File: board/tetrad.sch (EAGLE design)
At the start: 128 parts, among them Q1 FET-PCH-TO252, Q10 FET-NCH-SOT23, Q11 FET-NCH-SOT23, Q12 FET-NCH-SOT23, Q2 FET-NCH-SOT23, Q3 FET-NCH-SOT23, Q4 FET-NCH-SOT23, Q5 FET-NCH-SOT23, Q6 FET-NCH-SOT23, Q7 FET-NCH-SOT23, Q8 FET-NCH-SOT23, Q9 FET-NCH-SOT23, U1 IO-MCP23017ML, U2 RADIO-ESP32_DEVKIT, U3 R-78E5.0-1.0

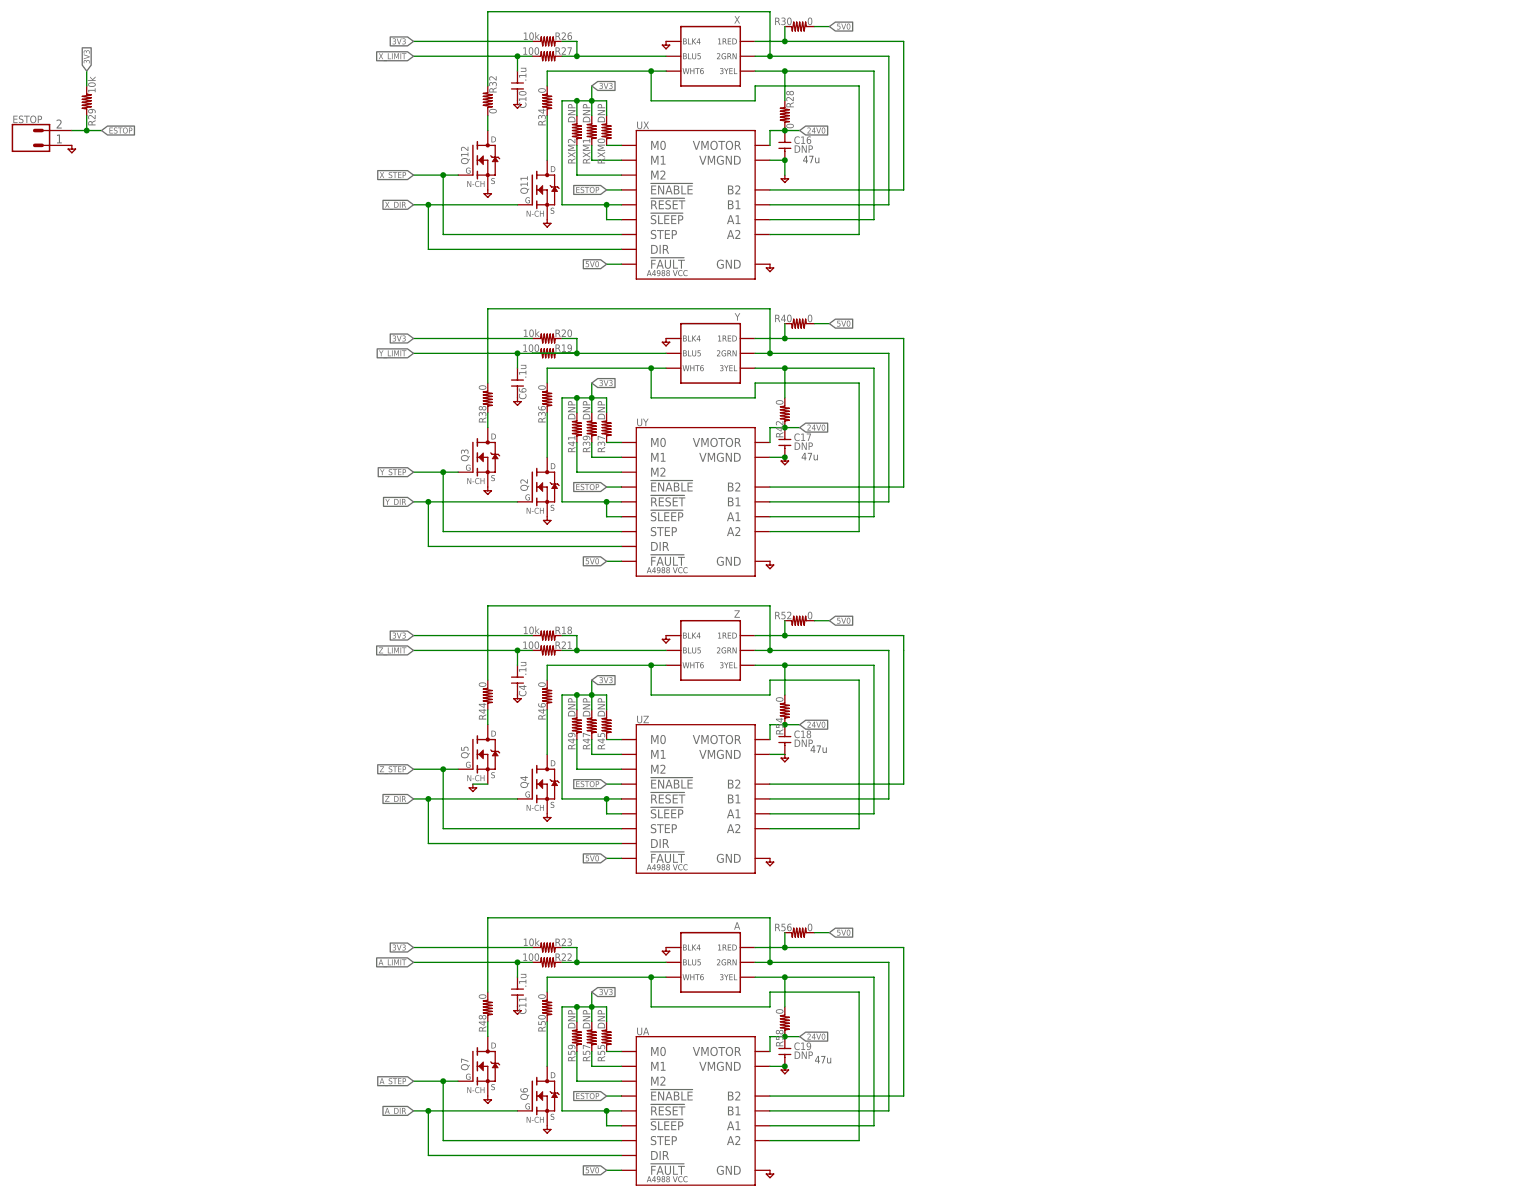
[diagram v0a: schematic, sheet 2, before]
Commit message: checked out the spindle hardware started to simplify the motor part of schematic
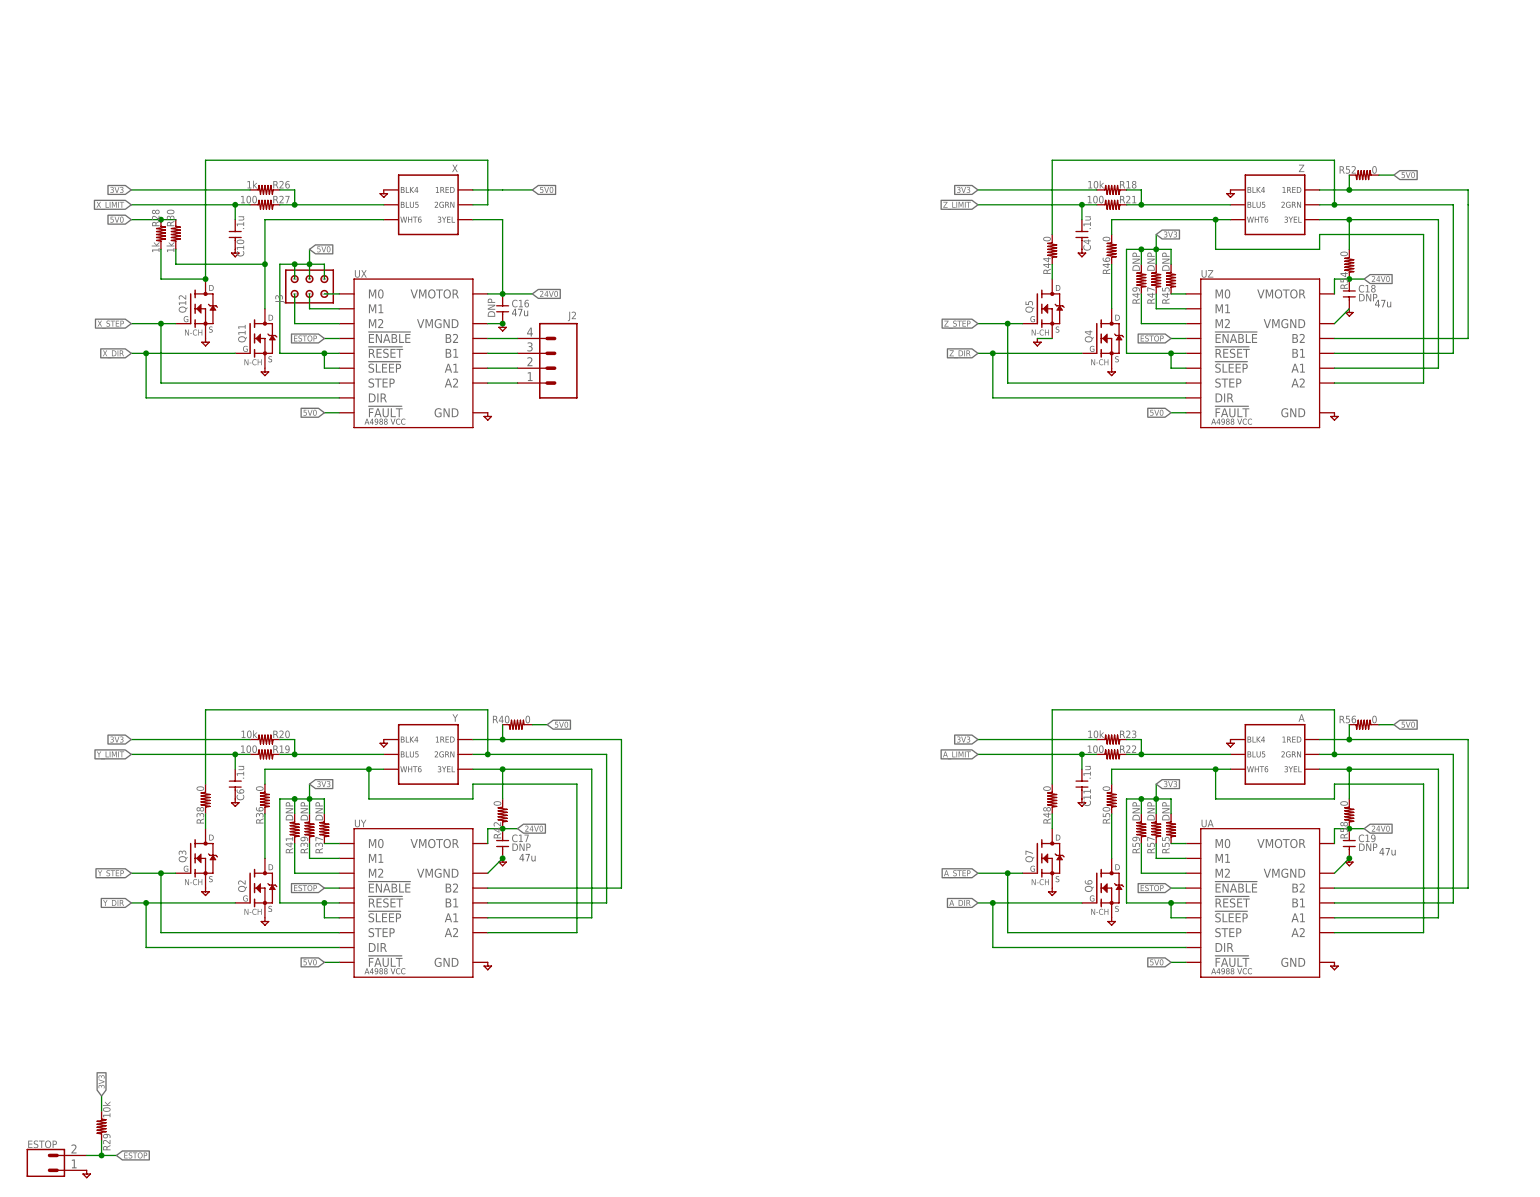
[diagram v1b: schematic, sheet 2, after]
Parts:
- removed R32, R34: 0, holla:R-0603
- removed RXM0, RXM1, RXM2: DNP, holla:R-0603
- added F1: 10A, holla:FUSE-HOLDER-3557-2
- added J2: (no value), holla:CONN-04-.100-VERT-HEADER
- added J3: (no value), holla:CONN-03X2-RH
- R26: value 10k -> 1k
- R28, R30: value 0 -> 1k
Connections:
- removed net N$30: R28.1, UX.A1, X.3
- removed net N$32: R30.1, UX.B2, X.1
- removed net N$44: Q12.D, R32.2
- new net N$57: F1.P$2, Q1.D
- new net N$62: J2.2, UX.A1
- new net N$63: J2.3, UX.B1
- new net N$64: J2.4, UX.B2
- net 24V0: now also X.3; no longer R28.2
- net 3V3: no longer RXM0.2, RXM1.2, RXM2.2, UX.!RESET, UX.!SLEEP
- net 5V0: now also J3.2, J3.4, J3.6, R28.1, R30.1, UX.!RESET, UX.!SLEEP, X.1; no longer R30.2
- net N$1: now also F1.P$1; no longer Q1.D
- net N$25: now also J2.1; no longer R34.2, X.6
- net N$31: now also Q12.D, R28.2; no longer R32.1, UX.B1
- net N$33: now also J3.5; no longer RXM0.1
- net N$34: now also J3.3; no longer RXM1.1
- net N$35: now also J3.1; no longer RXM2.1
- net N$5: now also R30.2, X.6; no longer R34.1
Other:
- note added: "todo add EVE2 display connector CS_SD is on an input only pin, fix this replace esp32 with new lib part, reroute check audio pin on FFC connector https://randomnerdtutorials.com/esp32-pinout-reference-gpios/ check if D14 and D15 PWM out on startup add 0430450612 headers add drv8825 board headers switch 23017 to qfn add strong pull ups to steps and dir add high current N-CH to extra 23107 outputs 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"
- note removed: "todo add EVE2 display connector CS_SD is on an input only pin, fix this replace esp32 with new lib part, reroute check audio pin on FFC connector https://randomnerdtutorials.com/esp32-pinout-reference-gpios/ check if D14 and D15 PWM out on startup add 0430450612 headers add drv8825 board headers switch 23017 to qfn add strong pull ups to steps and dir add high current N-CH to extra 23107 outputs"
- moved on the sheet: A, C10, C11, C14, C15, C16, C17, C18, C19, C4, C6, D1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

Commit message: schematic   updated alot   moving to bud PN-1325-DGMB enclosure initial add for others
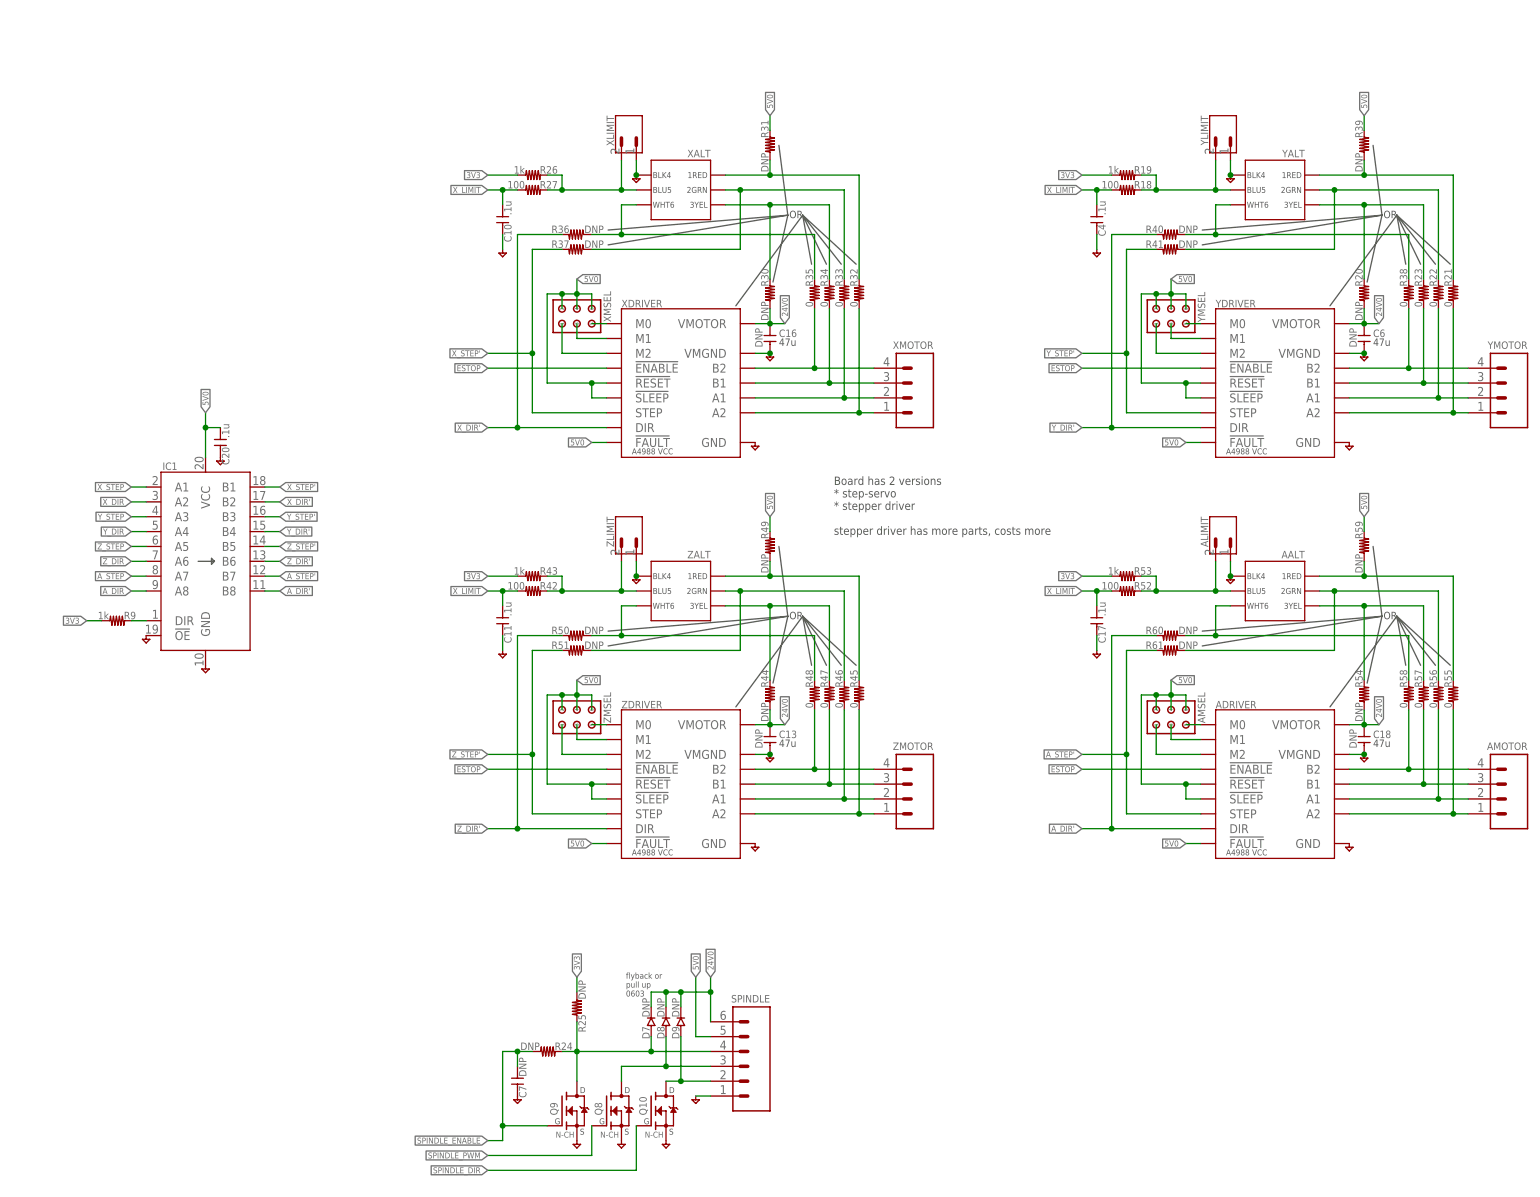
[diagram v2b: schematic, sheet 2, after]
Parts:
- removed 3V3: (no value), holla:TESTPOINTTHRU
- removed A, X, Y, Z: (no value), holla:CONN-03X2-MICROFIT-TH-SMD
- removed C19: DNP, holla:C-1206
- removed DISPLAY: (no value), holla:DISP-SPI-TFT-128X160-ST7735
- removed J3: (no value), holla:CONN-03X2-RH
- removed Q11, Q12, Q6, Q7: FET-NCH-SOT23, holla:FET-NCH-SOT23
- removed UA, UX, UY, UZ: (no value), holla:BOARD-DRV8825-CARRIER-TH-SMD
- added AALT, XALT, YALT, ZALT: (no value), holla:CONN-03X2-MICROFIT-TH-SMD
- added ADRIVER, XDRIVER, YDRIVER, ZDRIVER: (no value), holla:BOARD-DRV8825-CARRIER-TH-SMD
- added ALIMIT, XLIMIT, YLIMIT, ZLIMIT: (no value), holla:CONN-02-.100-VERT-HEADER
- added AMOTOR, XMOTOR, YMOTOR, ZMOTOR: (no value), holla:CONN-04-.100-VERT-HEADER
- added AMSEL, XMSEL, YMSEL, ZMSEL: (no value), holla:CONN-03X2-RH
- added AUDIO: (no value), holla:TESTPOINTTHRU
- added C20: .1u, holla:C-0603
- added D3, D4, D5, D6: (no value), holla:DIODE-0603-SOD523
- added D7, D8, D9: DNP, holla:DIODE-0603-SOD523
- added IC1: (no value), holla:74LS245DW
- added J16: (no value), holla:CONN-05X2-SHD
- added R31, R51, R60, R61: DNP, holla:R-0603
- added R32, R33, R34, R35: 0, holla:R-0603
- added R43, R53: 1k, holla:R-0603
- added U13: (no value), holla:CONN-20-FPC-0.50MM-10051922-2010ELF
- C1, C9: value 1u -> .1u
- C13: value 1u -> DNP; device holla:C-0603 -> holla:C-1206
- C17: value DNP -> .1u; device holla:C-1206 -> holla:C-0603
- C6: value .1u -> DNP; device holla:C-0603 -> holla:C-1206
- J2: device holla:CONN-04-.100-VERT-HEADER -> holla:CONN-06-3.81MM-PLUGIN-SCREW
- Q2, Q3, Q4, Q5: value FET-NCH-SOT23 -> FET-NCH-TO252; device holla:FET-NCH-SOT23 -> holla:FET-NCH-TO252
- R18: value 10k -> 100
- R19, R9: value 100 -> 1k
- R20: value 10k -> DNP
- R21, R22, R8: value 100 -> 0
- R23: value 10k -> 0
- R28: value 1k -> 100
- R30: value 1k -> DNP
- R36, R40, R44, R50, R54: value 0 -> DNP
- R42, R52: value 0 -> 100
- R45, R47, R55, R57: value DNP -> 0
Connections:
- new net A_DIR': ADRIVER.DIR, IC1.B8, R60.1
- new net A_STEP': ADRIVER.STEP, IC1.B7, R61.1
- new net N$108: R8.2, U13.3, U13.4
- new net N$30: D5.A, J2.3, Q4.D
- new net N$32: D4.A, J2.4, Q3.D
- new net N$44: D3.A, J2.5, Q2.D
- new net N$61: ADRIVER.M1, AMSEL.3
- new net N$65: ADRIVER.A1, AMOTOR.2, R56.2
- new net N$66: ADRIVER.B1, AMOTOR.3, R57.2
- new net N$67: ADRIVER.B2, AMOTOR.4, R58.2
- new net N$68: AALT.5, ALIMIT.2, R52.1, R53.1
- new net N$69: AALT.6, R58.1, R60.2
- new net N$70: AALT.1, R55.1, R59.2
- new net N$71: AALT.3, R54.1, R57.1
- new net X_DIR': IC1.B2, R36.1, XDRIVER.DIR
- new net X_STEP': IC1.B1, R22.1, R33.1, R37.1, R37.2, R41.2, R46.1, R51.2, XALT.2, XDRIVER.STEP, YALT.2, ZALT.2
- new net X_STEP'1: AALT.2, R56.1, R61.2
- new net Y_DIR': IC1.B4, R40.1, YDRIVER.DIR
- new net Y_STEP': IC1.B3, R41.1, YDRIVER.STEP
- new net Z_DIR': IC1.B6, R50.1, ZDRIVER.DIR
- new net Z_STEP': IC1.B5, R51.1, ZDRIVER.STEP
- net 24V0: now also ADRIVER.VMOTOR, C13.1, C6.1, D3.C, D4.C, D5.C, D6.C, D7.C, D8.C, D9.C, J2.6, R20.2, R30.2, R44.2, R54.2, XDRIVER.VMOTOR, YDRIVER.VMOTOR, ZDRIVER.VMOTOR; no longer C17.1, C19.1, R42.1, R54.1, R58.1, UA.VMOTOR, UX.VMOTOR, UY.VMOTOR, UZ.VMOTOR, X.3
- net 3V3: now also C1.1, C9.1, J16.1, R19.2, R43.2, R53.2, R8.1, R9.2, U13.20, U13.5; no longer 3V3.P$1, C1.2, C13.2, C9.2, R18.2, R20.2, R23.2, R37.2, R39.2, R41.2, R45.2, R47.2, R49.2, R55.2, R57.2, R59.2, UA.!RESET, UA.!SLEEP, UY.!RESET, UY.!SLEEP, UZ.!RESET, UZ.!SLEEP
- net 5V0: now also ADRIVER.!FAULT, ADRIVER.!RESET, ADRIVER.!SLEEP, AMSEL.2, AMSEL.4, AMSEL.6, C20.1, IC1.VCC, R31.1, R39.1, R49.1, R59.1, XDRIVER.!FAULT, XDRIVER.!RESET, XDRIVER.!SLEEP, XMSEL.2, XMSEL.4, XMSEL.6, YDRIVER.!FAULT, YDRIVER.!RESET, YDRIVER.!SLEEP, YMSEL.2, YMSEL.4, YMSEL.6, ZDRIVER.!FAULT, ZDRIVER.!RESET, ZDRIVER.!SLEEP, ZMSEL.2, ZMSEL.4, ZMSEL.6; no longer DISPLAY.VCC, J3.2, J3.4, J3.6, R28.1, R30.1, R40.2, R52.2, R56.2, UA.!FAULT, UX.!FAULT, UX.!RESET, UX.!SLEEP, UY.!FAULT, UZ.!FAULT, X.1
- net AUDIO: now also AUDIO.P$1, J16.9, U13.11
- net A_DIR: now also IC1.A8; no longer Q6.G, UA.DIR
- net A_LIMIT: no longer C11.1, R22.2
- net A_STEP: now also IC1.A7; no longer Q7.G, UA.STEP
- net CS_DISPLAY: now also J16.6, U13.15
- net CYCLE_START: now also U2.D39_IN_ONLY/VN; no longer U2.D39/VN
- net DISPLAY_CS: no longer DISPLAY.CS
- net DISPLAY_DC: no longer DISPLAY.DC
- net ESTOP: now also ADRIVER.!ENABLE, R28.1, XDRIVER.!ENABLE, YDRIVER.!ENABLE, ZDRIVER.!ENABLE; no longer UA.!ENABLE, UX.!ENABLE, UY.!ENABLE, UZ.!ENABLE
- net FEED_HOLD: now also U2.D36_IN_ONLY/VP; no longer U2.D36/VP
- net GND: now also AALT.4, ADRIVER.GND, ADRIVER.VMGND, ALIMIT.1, C1.2, C13.2, C20.2, C9.2, IC1.!OE, IC1.GND, J16.10, J16.2, J2.1, U13.1, U13.19, U13.2, U13.6, U13.G, XALT.4, XDRIVER.GND, XDRIVER.VMGND, XLIMIT.1, YALT.4, YDRIVER.GND, YDRIVER.VMGND, YLIMIT.1, ZALT.4, ZDRIVER.GND, ZDRIVER.VMGND, ZLIMIT.1; no longer A.4, C1.1, C13.1, C19.2, C9.1, DISPLAY.GND, Q11.S, Q12.S, Q6.S, Q7.S, UA.GND, UA.VMGND, UX.GND, UX.VMGND, UY.GND, UY.VMGND, UZ.GND, UZ.VMGND, X.4, Y.4, Z.4
- net INT_DISPLAY: now also J16.7, U13.14
- net MISO: now also J16.4, U13.17
- net MOSI: now also J16.5, U13.16; no longer R8.2
- net N$10: now also R22.2, YDRIVER.A1, YMOTOR.2; no longer A.5, R22.1, R23.1
- net N$11: now also R23.2, YDRIVER.B1, YMOTOR.3; no longer Q7.D, R48.1
- net N$13: now also D7.A
- net N$14: now also D9.A
- net N$18: now also R1.1
- net N$19: now also R7.1
- net N$2: now also R30.1, R34.1, XALT.3; no longer R26.1, R27.1, X.5
- net N$20: now also D6.A, J2.2, Q5.D; no longer DISPLAY.BL
- net N$21: now also R38.2, YDRIVER.B2, YMOTOR.4; no longer Q3.D, R38.1
- net N$25: now also R32.2, XDRIVER.A2, XMOTOR.1; no longer J2.1, UX.A2
- net N$3: now also IC1.DIR; no longer DISPLAY.SCLK
- net N$31: now also R18.1, R19.1, YALT.5, YLIMIT.2; no longer Q12.D, R28.2, X.2
- net N$33: now also XDRIVER.M0, XMSEL.5; no longer J3.5, UX.M0
- net N$34: now also XDRIVER.M1, XMSEL.3; no longer J3.3, UX.M1
- net N$35: now also XDRIVER.M2, XMSEL.1; no longer J3.1, UX.M2
- net N$36: now also R38.1, R40.2, YALT.6; no longer Q6.D, R50.1
- net N$37: now also R21.1, R39.2, YALT.1; no longer R37.1, UY.M0
- net N$38: now also R20.1, R23.1, YALT.3; no longer R39.1, UY.M1
- net N$39: now also R45.2, ZDRIVER.A2, ZMOTOR.1; no longer R41.1, UY.M2
- net N$4: now also R28.2; no longer DISPLAY.MOSI, R8.1
- net N$40: now also ZDRIVER.M0, ZMSEL.5; no longer R36.2, UY.A2, Y.6
- net N$41: now also ZDRIVER.M1, ZMSEL.3; no longer R42.2, UY.A1, Y.3
- net N$42: now also ZDRIVER.M2, ZMSEL.1; no longer R38.2, UY.B1, Y.2
- net N$43: now also R46.2, ZDRIVER.A1, ZMOTOR.2; no longer R40.1, UY.B2, Y.1
- net N$45: now also R47.2, ZDRIVER.B1, ZMOTOR.3; no longer R55.1, UA.M0
- net N$46: now also R48.2, ZDRIVER.B2, ZMOTOR.4; no longer R45.1, UZ.M0
- net N$47: now also R42.1, R43.1, ZALT.5, ZLIMIT.2; no longer R47.1, UZ.M1
- net N$48: now also R48.1, R50.2, ZALT.6; no longer R49.1, UZ.M2
- net N$49: now also R45.1, R49.2, ZALT.1; no longer R57.1, UA.M1
- net N$5: now also R31.2, R32.1, XALT.1; no longer Q11.D, R30.2, X.6
- net N$50: now also R47.1, ZALT.3; no longer Q5.D
- net N$51: now also ADRIVER.A2, AMOTOR.1, R55.2; no longer R46.2, UZ.A2, Z.6
- net N$52: now also Q2.G, U1.GPB4; no longer Q4.D, R46.1
- net N$53: now also Q3.G, U1.GPB5; no longer R44.2, UZ.B1, Z.2
- net N$54: now also Q4.G, U1.GPB6; no longer R54.2, UZ.A1, Z.3
- net N$55: now also Q5.G, U1.GPB7; no longer R59.1, UA.M2
- net N$56: now also R35.2, XDRIVER.B2, XMOTOR.4; no longer R52.1, UZ.B2, Z.1
- net N$58: now also R26.1, R27.1, XALT.5, XLIMIT.2; no longer A.6, R50.2, UA.A2
- net N$59: now also ADRIVER.M0, AMSEL.5; no longer A.3, R58.2, UA.A1
- net N$6: now also R21.2, YDRIVER.A2, YMOTOR.1; no longer R19.1, R20.1, Y.5
- net N$60: now also R35.1, R36.2, XALT.6; no longer A.2, R48.2, UA.B1
- net N$62: now also R33.2, XDRIVER.A1, XMOTOR.2; no longer J2.2, UX.A1
- net N$63: now also R34.2, XDRIVER.B1, XMOTOR.3; no longer J2.3, UX.B1
- net N$64: now also ADRIVER.M2, AMSEL.1; no longer J2.4, UX.B2
- net N$7: now also YDRIVER.M0, YMSEL.5; no longer Q2.D, R36.1
- net N$8: now also YDRIVER.M1, YMSEL.3; no longer R18.1, R21.1, Z.5
- net N$9: now also YDRIVER.M2, YMSEL.1; no longer A.1, R56.1, UA.B2
- net PD_DISPLAY: now also J16.8, U13.13
- net RESET: no longer DISPLAY.RESET
- net SCK: now also J16.3, U13.18; no longer R9.2
- net SCL: no longer R1.1
- net SDA: no longer R7.1
- net X_DIR: now also IC1.A2; no longer Q11.G, UX.DIR
- net X_LIMIT: now also C11.1, C17.1, C4.1, R18.2, R42.2, R52.2
- net X_STEP: now also IC1.A1; no longer Q12.G, UX.STEP
- net X_STEP_5V4: now also D8.A
- net Y_DIR: now also IC1.A4; no longer Q2.G, UY.DIR
- net Y_LIMIT: no longer C6.1, R19.2
- net Y_STEP: now also IC1.A3; no longer Q3.G, UY.STEP
- net Z_DIR: now also IC1.A6; no longer Q4.G, UZ.DIR
- net Z_LIMIT: no longer C4.1, R21.2
- net Z_STEP: now also IC1.A5; no longer Q5.G, UZ.STEP
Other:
- note added: "1 2 3 4 5 6 7 8 9 10 11 12 13 14 15 16 17 18 19 20"
- note added: "Board has 2 versions * step-servo * stepper driver stepper driver has more parts, costs more"
- note added: "Matrix Orbital EVE2-70G-TPC FFC 20P-0.5mm bottom connector flipped 1-20, 2-19, etc"
- note added: "New Haven NHD-7.0-800480FT-CSXV-CTP FFC 20P-1.0mm top"
- note added: "OR"
- note added: "flyback"
- note added: "flyback or pull up 0603"
- note added: "todo reroute check if D14 and D15 PWM out on startup check stepper motor config pins for drv8825 and trinamic switch 23017 to qfn add strong pull ups to steps and dir add high current N-CH to extra 23107 outputs estop polarity wrong on motor drivers references https://randomnerdtutorials.com/esp32-pinout-reference-gpios/"
- note removed: "todo add EVE2 display connector CS_SD is on an input only pin, fix this replace esp32 with new lib part, reroute check audio pin on FFC connector https://randomnerdtutorials.com/esp32-pinout-reference-gpios/ check if D14 and D15 PWM out on startup add 0430450612 headers add drv8825 board headers switch 23017 to qfn add strong pull ups to steps and dir add high current N-CH to extra 23107 outputs 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"
- moved on the sheet: C10, C11, C12, C16, C17, C18, C3, C4, C5, C6, C8, C9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
